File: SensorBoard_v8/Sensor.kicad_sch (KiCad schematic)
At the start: 43 parts, among them J11 TF-Luna2, J12 TF-Luna3, J13 TF-Luna1, J14 Bump_Center, J5 AnalogIR_Right, J6 AnalogIR_Center, J7 AnalogIR_Left, J8 AnalogIR_Extra, J9 LDROBOT_LD19, U5 ESP8266-1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

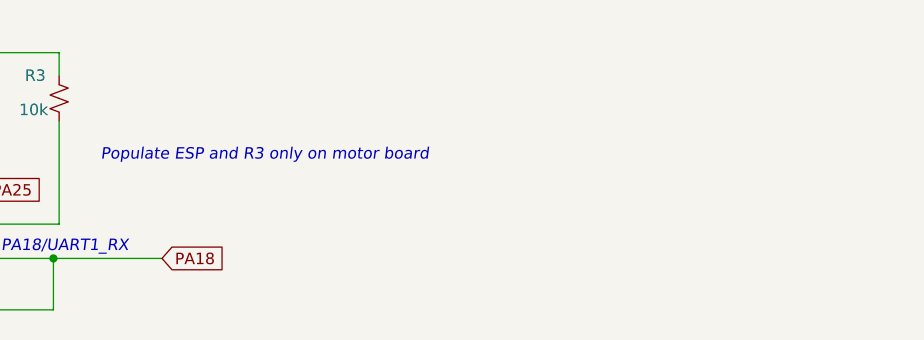
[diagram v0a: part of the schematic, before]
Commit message: added lab 6 update starter files
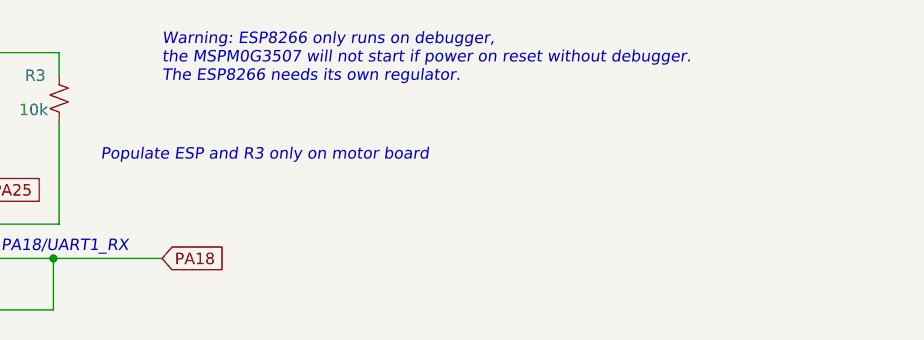
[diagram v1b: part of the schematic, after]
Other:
- note added: "Warning: ESP8266 only runs on debugger, the MSPM0G3507 will not start if power on reset without debugger. The ESP8266 needs its own regulator."
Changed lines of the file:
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@@
+		)
+	)
+	(text "Warning: ESP8266 only runs on debugger, \nthe MSPM0G3507 will not start if power on reset without debugger.\nThe ESP8266 needs its own regulator."
+		(exclude_from_sim no)
+		(at 197.485 17.78 0)
+		(effects
+			(font
+				(size 1.27 1.27)
+				(italic yes)
+			)
+			(justify left)
 		)
 	)
